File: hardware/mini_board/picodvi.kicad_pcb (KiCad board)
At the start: 4 copper layers, 22.8 x 18.8 mm, 45 parts, among them J1 USB_A, J5 NOT_HDMI_A, SW1 SW_Push, SW2 SW_Push, U1 RP2040, U2 NCP115ASN330, U3 W25Q16JV, U4 S70KS128, Y1 12 M

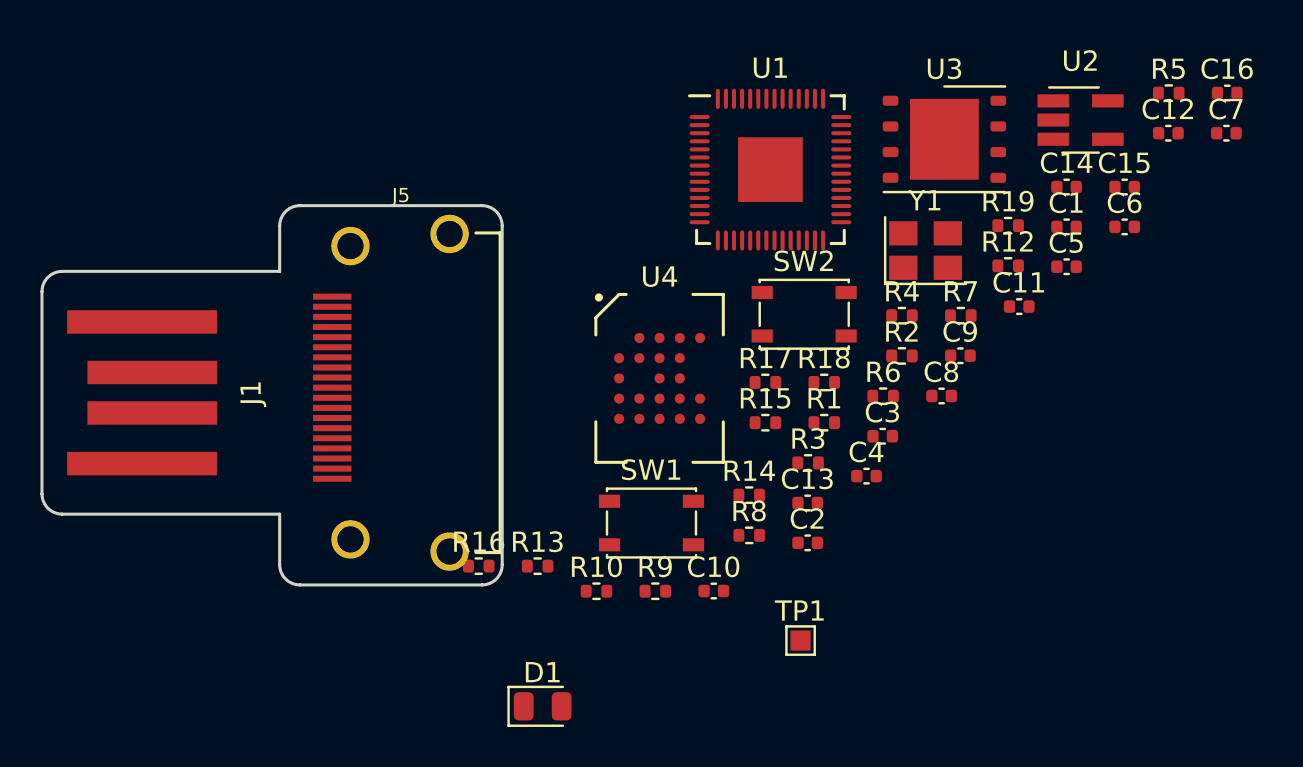
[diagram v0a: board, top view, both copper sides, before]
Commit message: Clean up kicad backup stuff in mini board directory
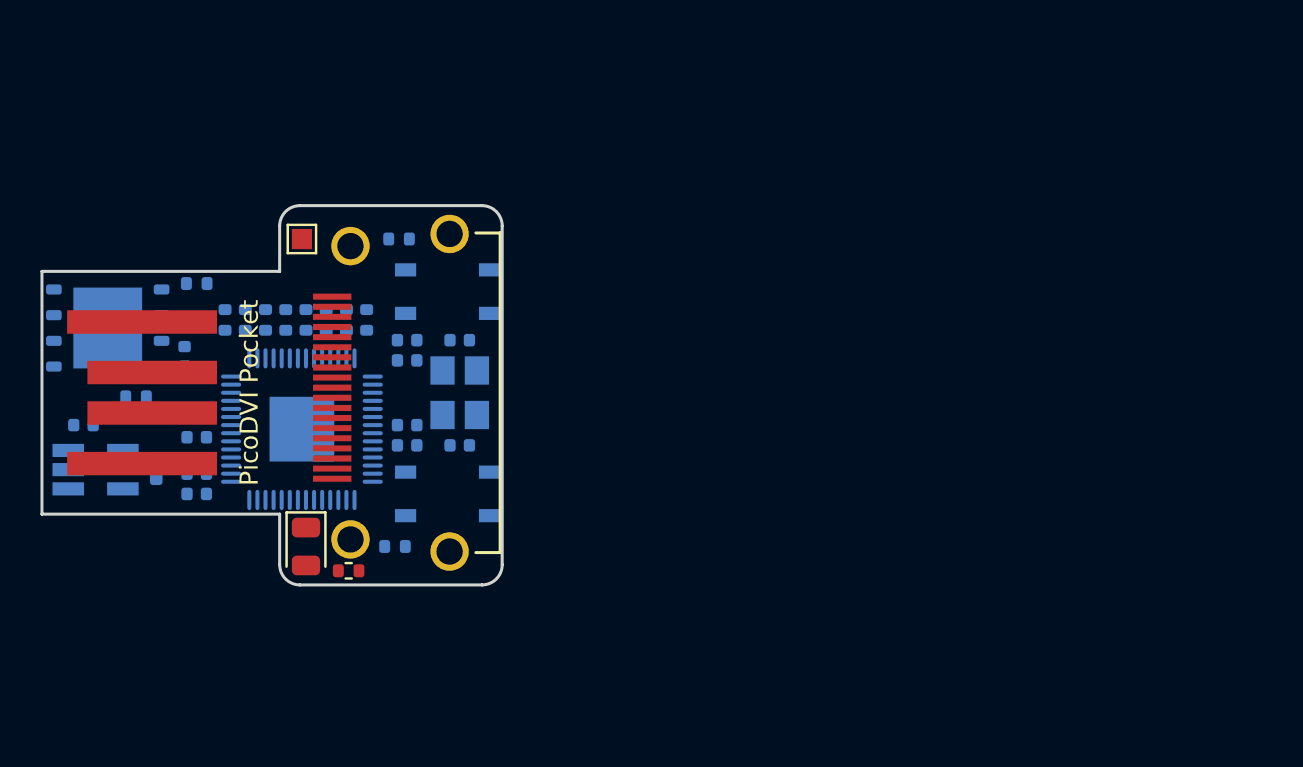
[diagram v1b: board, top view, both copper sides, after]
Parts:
- removed C14, C15, C16: 100n, Capacitor_SMD:C_0402_1005Metric
- removed R10: 270, Resistor_SMD:R_0402_1005Metric
- removed R7, R8, R9: 2k2, Resistor_SMD:R_0402_1005Metric
- removed U4: S70KS128, picodvi:S70KS128
- C1, C10, C11, C12, C13, C2, C3, C4, C5, C6, C7, C8, C9, R1, R12, R13, R14, R15, R16, R17, R18, R19, R2, R3, R4, R5, SW1, SW2, U1, U2, U3, Y1: moved to B.Cu
- moved C7 58.3 mm to (202.8, 111.6)
- moved R5 53.2 mm to (205.4, 110.2)
- moved U2 51.7 mm to (203.4, 113.8)
- moved C6 46.9 mm to (207.8, 108.2), turned to -90 degrees
- moved C1 46.6 mm to (206.4, 113.8), turned to 90 degrees
- moved U3 42.4 mm to (204.0, 106.8), turned to 180 degrees
- moved C11 41.7 mm to (208.4, 115.0), turned to 180 degrees
- moved C12 38.3 mm to (221.4, 112.6)
- moved R4 38.2 mm to (205.4, 111.2)
- moved R19 38.0 mm to (210.8, 106.4), turned to 90 degrees
- moved C8 36.8 mm to (208.4, 111.2), turned to 180 degrees
- moved C3 34.0 mm to (208.4, 114.0), turned to 180 degrees
- moved C5 33.8 mm to (218.8, 112.6)
- moved R12 31.8 mm to (216.8, 106.4), turned to -90 degrees
- moved TP1 31.6 mm to (213.6, 102.4)
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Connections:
- J5 pad 13: Net-(J5-Pad13) -> unconnected-(J5-Pad13)
- J5 pad 15: /uC_DVI_SCL -> unconnected-(J5-Pad15)
- J5 pad 16: /uC_DVI_SDA -> unconnected-(J5-Pad16)
- U1 pad 11: /HRAM_DQ7 -> /uC_DVI_D1-
- U1 pad 12: /HRAM_CK -> /uC_DVI_D1+
- U1 pad 13: /HRAM_~CS~ -> /uC_DVI_D2-
- U1 pad 14: /HRAM_RWDS -> /uC_DVI_D2+
- U1 pad 15: /uC_DVI_SDA -> unconnected-(U1-Pad15)
- U1 pad 16: /uC_DVI_SCL -> unconnected-(U1-Pad16)
- U1 pad 17: /uC_DVI_CEC -> /~USER_BUTTON~
- U1 pad 2: /~USER_BUTTON~ -> unconnected-(U1-Pad2)
- U1 pad 27: /uC_DVI_CK- -> unconnected-(U1-Pad27)
- U1 pad 28: /uC_DVI_CK+ -> unconnected-(U1-Pad28)
- U1 pad 29: /uC_DVI_D0- -> unconnected-(U1-Pad29)
- U1 pad 3: /HRAM_DQ0 -> unconnected-(U1-Pad3)
- U1 pad 30: /uC_DVI_D0+ -> unconnected-(U1-Pad30)
- U1 pad 31: /uC_DVI_D1- -> unconnected-(U1-Pad31)
- U1 pad 32: /uC_DVI_D1+ -> unconnected-(U1-Pad32)
- U1 pad 34: /uC_DVI_D2- -> unconnected-(U1-Pad34)
- U1 pad 35: /uC_DVI_D2+ -> unconnected-(U1-Pad35)
- U1 pad 36: /uC_DVI_SDA -> unconnected-(U1-Pad36)
- U1 pad 37: /uC_DVI_SCL -> unconnected-(U1-Pad37)
- U1 pad 38: /uC_DVI_CEC -> unconnected-(U1-Pad38)
- U1 pad 4: /HRAM_DQ1 -> unconnected-(U1-Pad4)
- U1 pad 41: /HRAM_~RST~ -> unconnected-(U1-Pad41)
- U1 pad 5: /HRAM_DQ2 -> unconnected-(U1-Pad5)
- U1 pad 6: /HRAM_DQ3 -> /uC_DVI_CK-
- U1 pad 7: /HRAM_DQ4 -> /uC_DVI_CK+
- U1 pad 8: /HRAM_DQ5 -> /uC_DVI_D0-
- U1 pad 9: /HRAM_DQ6 -> /uC_DVI_D0+
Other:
- outline, holes or cut-outs redrawn
- board text added: "PicoDVI Pocket"
